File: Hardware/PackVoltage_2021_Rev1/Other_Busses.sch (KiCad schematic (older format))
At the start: 40 parts, among them Q5 Q_NMOS_DGS, Q6 Q_NMOS_DGS, Q7 Q_NMOS_DGS, Q8 Q_NMOS_DGS, U13 LT1910, U14 LT1910, U15 LT1910, U16 INA281, U17 INA281, U18 INA281, U19 LT1910, U20 INA281

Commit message: Renaming Extra Bus, Fixing Fuse Values
Renamed Extra 6 bus to Auxiliary 1 and moved it from Motor Busses to Other Busses
Changed Fuse values on Other Busses from 15 for all to 25 for Aux, Spare, and Rocket, to 10 for Vacuum, and to 20 for 12V
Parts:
- added C?: 0.1uF, symbol Device:C_Small
- added C?: 10uF, symbol Device:C_Small
- added D?: LED, symbol Device:LED
- added F?: 25, symbol Device:Fuse
- added Q?: Q_NMOS_DGS, symbol Device:Q_NMOS_DGS
- added R?: 5.1k, symbol Device:R
- added R?: 0.05, symbol Device:R
- added R?: 3300, symbol Device:R
- added U?: INA281, symbol MRDT_ICs:INA281
- added U?: LT1910, symbol MRDT_ICs:LT1910
- F5: value 15 -> 20
- F6: value 15 -> 10
- F7, F8: value 15 -> 25
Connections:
- net 5V: now also R?.2, U?.5 (V+)
- net GND: now also C?.2, C?.2, R?.2, U?.1 (GND), U?.2 (GND)
- net PV: now also F?.1
- new net: C?.1, F?.2, Q?.1 (D), U?.6 (SENSE), U?.8 (V+)
- new net: Q?.2 (G), U?.5 (GATE)
- new net: R?.1, U?.3 (FAULT)
- new net: C?.1, U?.2 (TIMER)
- new net: R?.2, U?.4 (-)
- new net: D?.1 (K), R?.1
- new net Anderson_A1: D?.2 (A), Q?.3 (S), R?.1, U?.3 (+)
- new net Current_Sensor_A1: U?.1
- new net Driver_A1: U?.4 (IN)
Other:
- note added: "Auxiliary"

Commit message: Fixed anderson connections
Mistake made when rearranging busses so they would fit on sheet fixed
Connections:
- net Anderson_A1: now also R?.2, U?.4 (-); no longer D?.2 (A), Q?.3 (S), R?.1, U?.3 (+)
- net Anderson_R1: now also R21.2, U18.4 (-); no longer D15.2 (A), Q7.3 (S), R21.1, U18.3 (+)
- net Anderson_S1: now also R26.2, U20.4 (-); no longer D16.2 (A), Q8.3 (S), R26.1, U20.3 (+)
- net Anderson_T1: now also R19.2, U16.4 (-); no longer D13.2 (A), Q5.3 (S), R19.1, U16.3 (+)
- net Anderson_V1: now also R20.2, U17.4 (-); no longer D14.2 (A), Q6.3 (S), R20.1, U17.3 (+)
- new net: D15.2 (A), Q7.3 (S), R21.1, U18.3 (+)
- new net: D14.2 (A), Q6.3 (S), R20.1, U17.3 (+)
- new net: D16.2 (A), Q8.3 (S), R26.1, U20.3 (+)
- new net: D?.2 (A), Q?.3 (S), R?.1, U?.3 (+)
- new net: D13.2 (A), Q5.3 (S), R19.1, U16.3 (+)
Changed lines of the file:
@@
 Connection ~ 3100 1850
 Wire Wire Line
-	3550 1950 3900 1950
-Wire Wire Line
-	3100 1850 3100 2100
-Wire Wire Line
-	3100 2100 3350 2100
-Connection ~ 3100 2100
-Wire Wire Line
-	3100 2100 3100 2300
+	3550 1950 3750 1950
+Wire Wire Line
+	3750 2100 4000 2100
 Text HLabel 4500 1450 1    50   Output ~ 0
 Current_Sensor_R1
@@
 Connection ~ 3050 3850
 Wire Wire Line
-	3500 3950 3850 3950
-Wire Wire Line
-	3050 3850 3050 4100
-Wire Wire Line
-	3050 4100 3300 4100
-Connection ~ 3050 4100
-Wire Wire Line
-	3050 4100 3050 4300
+	3500 3950 3700 3950
+Wire Wire Line
+	3700 4100 3950 4100
 Text HLabel 4450 3450 1    50   Output ~ 0
 Current_Sensor_T1
@@
 Connection ~ 3050 6050
 Wire Wire Line
-	3500 6150 3850 6150
-Wire Wire Line
-	3050 6050 3050 6300
-Wire Wire Line
-	3050 6300 3300 6300
-Connection ~ 3050 6300
-Wire Wire Line
-	3050 6300 3050 6500
+	3500 6150 3700 6150
+Wire Wire Line
+	3700 6300 3950 6300
 Text HLabel 4450 5650 1    50   Output ~ 0
 Current_Sensor_V1
@@
 Connection ~ 8450 1900
 Wire Wire Line
-	8900 2000 9250 2000
-Wire Wire Line
-	8450 1900 8450 2150
-Wire Wire Line
-	8450 2150 8700 2150
-Connection ~ 8450 2150
-Wire Wire Line
-	8450 2150 8450 2350
+	8900 2000 9100 2000
+Wire Wire Line
+	9100 2150 9350 2150
 Text HLabel 9850 1500 1    50   Output ~ 0
 Current_Sensor_S1
@@
 	1    0    0    -1
 $EndComp
-Text HLabel 3350 2100 2    50   Output ~ 0
+Text HLabel 4000 2100 2    50   Output ~ 0
 Anderson_R1
-Text HLabel 3300 4100 2    50   Output ~ 0
+Text HLabel 3950 4100 2    50   Output ~ 0
 Anderson_T1
-Text HLabel 3300 6300 2    50   Output ~ 0
+Text HLabel 3950 6300 2    50   Output ~ 0
 Anderson_V1
-Text HLabel 8700 2150 2    50   Output ~ 0
+Text HLabel 9350 2150 2    50   Output ~ 0
 Anderson_S1
 $Comp
@@
 Connection ~ 8450 3950
 Wire Wire Line
-	8900 4050 9250 4050
-Wire Wire Line
-	8450 3950 8450 4200
-Wire Wire Line
-	8450 4200 8700 4200
-Connection ~ 8450 4200
-Wire Wire Line
-	8450 4200 8450 4400
+	8900 4050 9100 4050
+Wire Wire Line
+	9100 4200 9350 4200
 Text HLabel 9850 3550 1    50   Output ~ 0
 Current_Sensor_A1
-Text HLabel 8700 4200 2    50   Output ~ 0
+Text HLabel 9350 4200 2    50   Output ~ 0
 Anderson_A1
+Wire Wire Line
+	3100 1850 3100 2300
+Wire Wire Line
+	3750 2100 3750 1950
+Connection ~ 3750 1950
+Wire Wire Line
+	3750 1950 3900 1950
+Wire Wire Line
+	3050 3850 3050 4300
+Wire Wire Line
+	3700 4100 3700 3950
+Connection ~ 3700 3950
+Wire Wire Line
+	3700 3950 3850 3950
+Wire Wire Line
+	3050 6050 3050 6500
+Wire Wire Line
+	3700 6300 3700 6150
+Connection ~ 3700 6150
+Wire Wire Line
+	3700 6150 3850 6150
+Wire Wire Line
+	8450 3950 8450 4400
+Wire Wire Line
+	9100 4200 9100 4050
+Connection ~ 9100 4050
+Wire Wire Line
+	9100 4050 9250 4050
+Wire Wire Line
+	8450 1900 8450 2350
+Wire Wire Line
+	9100 2150 9100 2000
+Connection ~ 9100 2000
+Wire Wire Line
+	9100 2000 9250 2000
 $EndSCHEMATC

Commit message: updated busses, fuses, and some names
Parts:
- F7: value 25 -> 15
- F8: value 25 -> 20
- F9: renamed from F?; value 25 -> 20
- gave numbers to parts that had none: 8
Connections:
- net Anderson_S1 renamed Anderson_D1
- net Current_Sensor_S1 renamed Current_Sensor_D1
- net Driver_E1 renamed Driver_V1
- net Driver_S1 renamed Driver_D1
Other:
- note added: "Driveboard"
- note removed: "Spare"
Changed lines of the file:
@@
 $Descr A4 11693 8268
 encoding utf-8
-Sheet 5 5
+Sheet 4 5
 Title ""
 Date ""
@@
 	4450 5750 4450 5650
 Text HLabel 1050 5850 0    50   Input ~ 0
-Driver_E1
+Driver_V1
 Wire Wire Line
 	3050 6050 3300 6050
@@
 AR Path="/5F8EFCC9/5F8B2B23" Ref="F8"  Part="1"
 F 0 "F8" V 7750 1250 50  0000 L CNN
-F 1 "25" V 7850 1250 50  0000 L CNN
+F 1 "20" V 7850 1250 50  0000 L CNN
 F 2 "" V 7780 1300 50  0001 C CNN
 F 3 "~" H 7850 1300 50  0001 C CNN
@@
 Connection ~ 7950 1550
 Text Notes 7500 900  0    157  ~ 0
-Spare
+Driveboard
 Wire Wire Line
 	8700 1900 8700 1500
@@
 	9850 1600 9850 1500
 Text HLabel 6450 1700 0    50   Input ~ 0
-Driver_S1
+Driver_D1
 Wire Wire Line
 	8450 1900 8700 1900
@@
 	9100 2150 9350 2150
 Text HLabel 9850 1500 1    50   Output ~ 0
-Current_Sensor_S1
+Current_Sensor_D1
 $Comp
 L Device:Fuse F?
@@
 AR Path="/5F8EFCC9/5F78099C" Ref="F7"  Part="1"
 F 0 "F7" V 2400 1200 50  0000 L CNN
-F 1 "25" V 2500 1200 50  0000 L CNN
+F 1 "15" V 2500 1200 50  0000 L CNN
 F 2 "" V 2430 1250 50  0001 C CNN
 F 3 "~" H 2500 1250 50  0001 C CNN
@@
 Anderson_V1
 Text HLabel 9350 2150 2    50   Output ~ 0
-Anderson_S1
+Anderson_D1
 $Comp
 L Device:Q_NMOS_DGS Q?
@@
 P 7850 3350
 AR Path="/5F7A6A8B/5F8E41F3" Ref="F?"  Part="1"
-AR Path="/5F8EFCC9/5F8E41F3" Ref="F?"  Part="1"
-F 0 "F?" V 7750 3300 50  0000 L CNN
-F 1 "25" V 7850 3300 50  0000 L CNN
+AR Path="/5F8EFCC9/5F8E41F3" Ref="F9"  Part="1"
+F 0 "F9" V 7750 3300 50  0000 L CNN
+F 1 "20" V 7850 3300 50  0000 L CNN
 F 2 "" V 7780 3350 50  0001 C CNN
 F 3 "~" H 7850 3350 50  0001 C CNN
@@
 P 6300 3600
 AR Path="/5F7A6A8B/5F8E41F9" Ref="R?"  Part="1"
-AR Path="/5F8EFCC9/5F8E41F9" Ref="R?"  Part="1"
-F 0 "R?" V 6200 3600 50  0000 C CNN
+AR Path="/5F8EFCC9/5F8E41F9" Ref="R28"  Part="1"
+F 0 "R28" V 6200 3600 50  0000 C CNN
 F 1 "5.1k" V 6300 3600 50  0000 C CNN
 F 2 "" V 6230 3600 50  0001 C CNN
@@
 P 6600 4100
 AR Path="/5F7A6A8B/5F8E4206" Ref="C?"  Part="1"
-AR Path="/5F8EFCC9/5F8E4206" Ref="C?"  Part="1"
-F 0 "C?" H 6692 4146 50  0000 L CNN
+AR Path="/5F8EFCC9/5F8E4206" Ref="C27"  Part="1"
+F 0 "C27" H 6692 4146 50  0000 L CNN
 F 1 "0.1uF" H 6692 4055 50  0000 L CNN
 F 2 "" H 6600 4100 50  0001 C CNN
@@
 P 7950 4100
 AR Path="/5F7A6A8B/5F8E420E" Ref="C?"  Part="1"
-AR Path="/5F8EFCC9/5F8E420E" Ref="C?"  Part="1"
-F 0 "C?" H 8042 4146 50  0000 L CNN
+AR Path="/5F8EFCC9/5F8E420E" Ref="C28"  Part="1"
+F 0 "C28" H 8042 4146 50  0000 L CNN
 F 1 "10uF" H 8042 4055 50  0000 L CNN
 F 2 "" H 7950 4100 50  0001 C CNN
@@
 P 8900 3800
 AR Path="/5F7A6A8B/5F8E4229" Ref="R?"  Part="1"
-AR Path="/5F8EFCC9/5F8E4229" Ref="R?"  Part="1"
-F 0 "R?" V 8800 3750 50  0000 L CNN
+AR Path="/5F8EFCC9/5F8E4229" Ref="R29"  Part="1"
+F 0 "R29" V 8800 3750 50  0000 L CNN
 F 1 "0.05" V 8900 3700 50  0000 L CNN
 F 2 "" V 8830 3800 50  0001 C CNN
@@
 P 8850 4400
 AR Path="/5F7A6A8B/5F8E4236" Ref="D?"  Part="1"
-AR Path="/5F8EFCC9/5F8E4236" Ref="D?"  Part="1"
-F 0 "D?" H 8850 4500 50  0000 C CNN
+AR Path="/5F8EFCC9/5F8E4236" Ref="D17"  Part="1"
+F 0 "D17" H 8850 4500 50  0000 C CNN
 F 1 "LED" H 8850 4600 50  0000 C CNN
 F 2 "" H 8850 4400 50  0001 C CNN
@@
 P 9300 4400
 AR Path="/5F7A6A8B/5F8E423D" Ref="R?"  Part="1"
-AR Path="/5F8EFCC9/5F8E423D" Ref="R?"  Part="1"
-F 0 "R?" V 9200 4350 50  0000 L CNN
+AR Path="/5F8EFCC9/5F8E423D" Ref="R30"  Part="1"
+F 0 "R30" V 9200 4350 50  0000 L CNN
 F 1 "3300" V 9300 4300 50  0000 L CNN
 F 2 "" V 9230 4400 50  0001 C CNN
@@
 P 9450 3650
 AR Path="/5F7A6A8B/5F8E4246" Ref="U?"  Part="1"
-AR Path="/5F8EFCC9/5F8E4246" Ref="U?"  Part="1"
-F 0 "U?" H 9550 3950 50  0000 L CNN
+AR Path="/5F8EFCC9/5F8E4246" Ref="U22"  Part="1"
+F 0 "U22" H 9550 3950 50  0000 L CNN
 F 1 "INA281" H 9500 3850 50  0000 L CNN
 F 2 "" H 9700 3850 50  0001 C CNN
@@
 P 6800 4000
 AR Path="/5F7A6A8B/5F8E424C" Ref="U?"  Part="1"
-AR Path="/5F8EFCC9/5F8E424C" Ref="U?"  Part="1"
-F 0 "U?" H 7175 4687 60  0000 C CNN
+AR Path="/5F8EFCC9/5F8E424C" Ref="U21"  Part="1"
+F 0 "U21" H 7175 4687 60  0000 C CNN
 F 1 "LT1910" H 7175 4581 60  0000 C CNN
 F 2 "" H 6800 4000 60  0001 C CNN

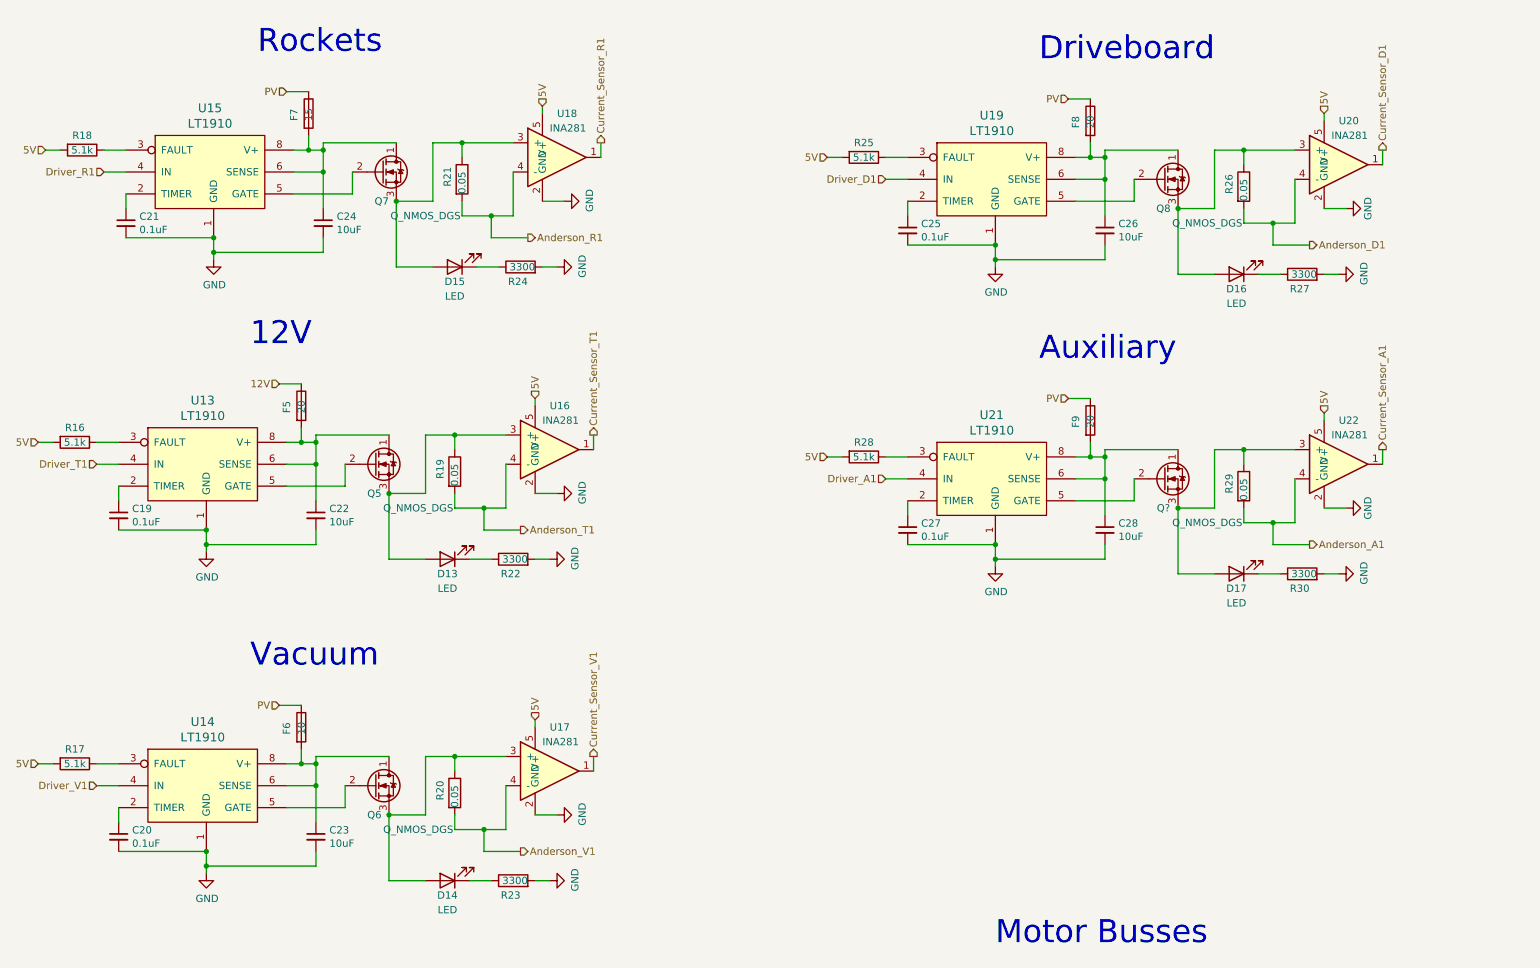
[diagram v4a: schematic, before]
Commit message: corrected orientation of ground symbols, renamed buck converters, still need to update tiva with extra 12V pin
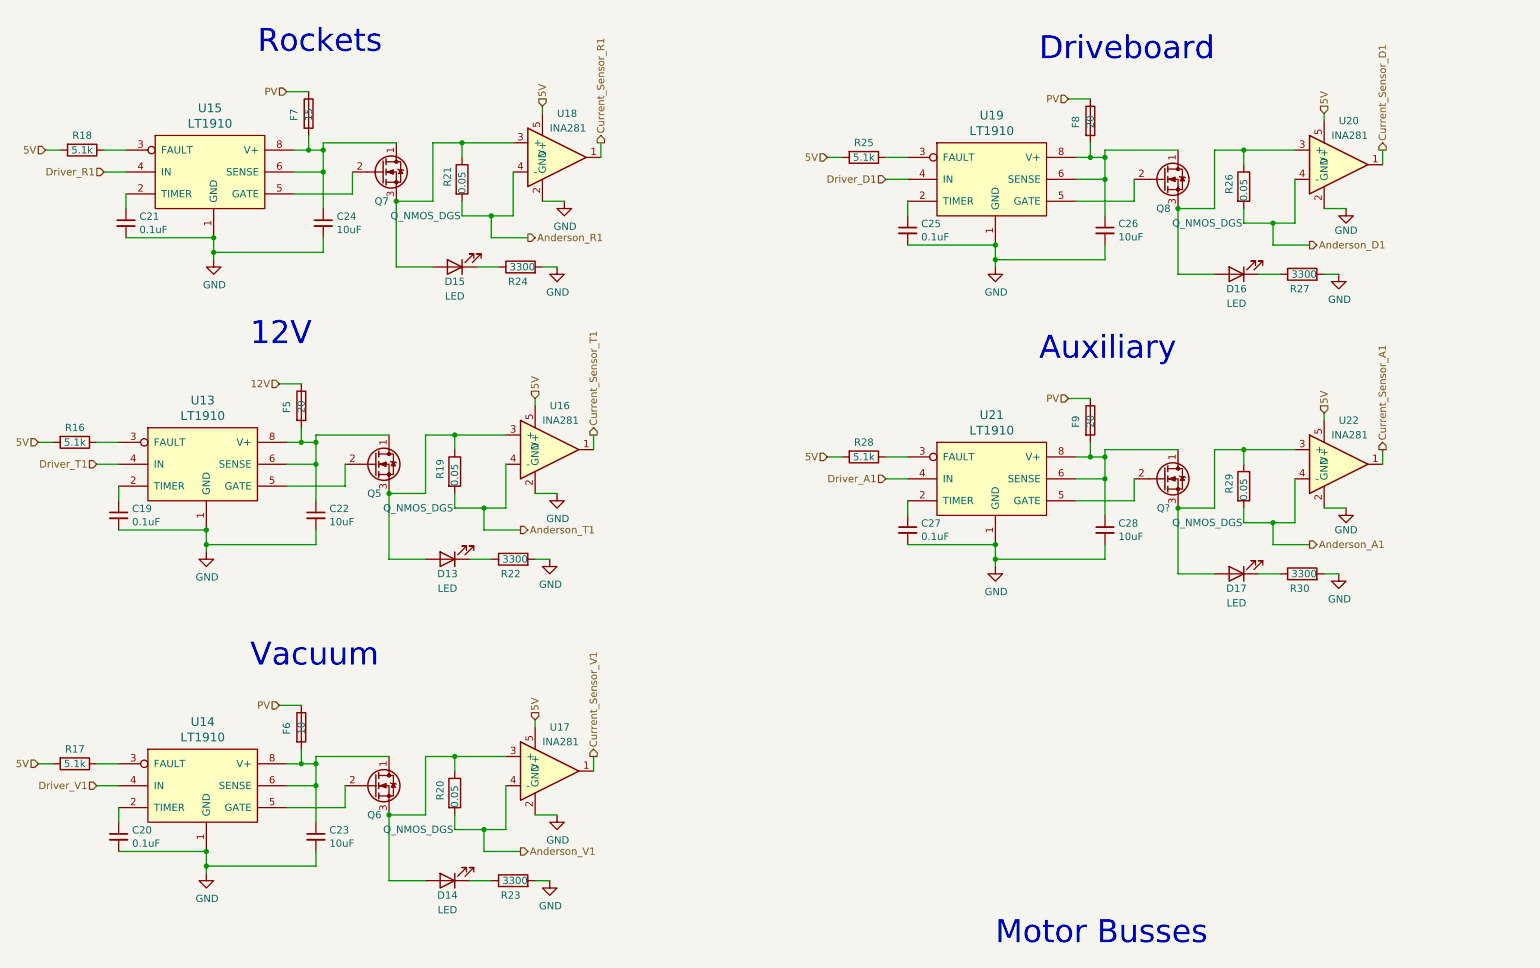
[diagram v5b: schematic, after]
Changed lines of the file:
@@
 F 3 "" H 4250 1850 50  0001 C CNN
 	1    4250 1850
-	0    -1   -1   0
+	1    0    0    -1
 $EndComp
 $Comp
@@
 F 3 "" H 4200 2300 50  0001 C CNN
 	1    4200 2300
-	0    -1   -1   0
+	1    0    0    -1
 $EndComp
 Connection ~ 3100 1850
@@
 F 3 "" H 4200 3850 50  0001 C CNN
 	1    4200 3850
-	0    -1   -1   0
+	1    0    0    -1
 $EndComp
 $Comp
@@
 F 3 "" H 4150 4300 50  0001 C CNN
 	1    4150 4300
-	0    -1   -1   0
+	1    0    0    -1
 $EndComp
 Connection ~ 3050 3850
@@
 F 3 "" H 4200 6050 50  0001 C CNN
 	1    4200 6050
-	0    -1   -1   0
+	1    0    0    -1
 $EndComp
 $Comp
@@
 F 3 "" H 4150 6500 50  0001 C CNN
 	1    4150 6500
-	0    -1   -1   0
+	1    0    0    -1
 $EndComp
 Connection ~ 3050 6050
@@
 F 3 "" H 9600 1900 50  0001 C CNN
 	1    9600 1900
-	0    -1   -1   0
+	1    0    0    -1
 $EndComp
 $Comp
@@
 F 3 "" H 9550 2350 50  0001 C CNN
 	1    9550 2350
-	0    -1   -1   0
+	1    0    0    -1
 $EndComp
 Connection ~ 8450 1900
@@
 F 3 "" H 9600 3950 50  0001 C CNN
 	1    9600 3950
-	0    -1   -1   0
+	1    0    0    -1
 $EndComp
 $Comp
@@
 F 3 "" H 9550 4400 50  0001 C CNN
 	1    9550 4400
-	0    -1   -1   0
+	1    0    0    -1
 $EndComp
 Connection ~ 8450 3950

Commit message: Updated molex connector (Still need tiva pin)
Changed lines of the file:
@@
 Wire Wire Line
 	3350 1850 3350 1450
-Wire Wire Line
-	3550 1450 3900 1450
 Connection ~ 3550 1450
 Wire Wire Line
@@
 	1    0    0    -1
 $EndComp
-Wire Wire Line
-	4100 1850 4250 1850
 $Comp
 L power:GND #PWR?
@@
 Wire Wire Line
 	4100 2300 4200 2300
-Text HLabel 2350 1100 0    50   Input ~ 0
+Text HLabel 2350 1100 1    50   Input ~ 0
 PV
-$Comp
-L MRDT_ICs:INA281 U?
-U 1 1 5F9AF7BB
-P 4100 1550
-AR Path="/5F7A6A8B/5F9AF7BB" Ref="U?"  Part="1"
-AR Path="/5F8EFCC9/5F9AF7BB" Ref="U18"  Part="1"
-F 0 "U18" H 4200 1850 50  0000 L CNN
-F 1 "INA281" H 4150 1750 50  0000 L CNN
-F 2 "" H 4350 1750 50  0001 C CNN
-F 3 "" H 4350 1750 50  0001 C CNN
-	1    4100 1550
-	1    0    0    -1
-$EndComp
 $Comp
 L MRDT_ICs:LT1910 U?
@@
 Text HLabel 4100 1200 1    50   Input ~ 0
 5V
-Text HLabel 700  1500 0    50   Input ~ 0
-5V
 Wire Wire Line
 	700  1500 800  1500
 Wire Wire Line
 	4100 1200 4100 1250
-Wire Wire Line
-	4500 1550 4500 1450
 Text HLabel 1100 1650 0    50   Input ~ 0
 Driver_R1
@@
 Wire Wire Line
 	3750 2100 4000 2100
-Text HLabel 4500 1450 1    50   Output ~ 0
-Current_Sensor_R1
 $Comp
 L Device:Q_NMOS_DGS Q?
@@
 Wire Wire Line
 	4050 4300 4150 4300
-Text HLabel 2300 3100 0    50   Input ~ 0
+Text HLabel 2300 3100 1    50   Input ~ 0
 12V
 $Comp
@@
 Text HLabel 4050 3200 1    50   Input ~ 0
 5V
-Text HLabel 650  3500 0    50   Input ~ 0
-5V
 Wire Wire Line
 	650  3500 750  3500
 Wire Wire Line
 	4050 3200 4050 3250
-Wire Wire Line
-	4450 3550 4450 3450
 Text HLabel 1050 3650 0    50   Input ~ 0
 Driver_T1
@@
 Wire Wire Line
 	3700 4100 3950 4100
-Text HLabel 4450 3450 1    50   Output ~ 0
+Text HLabel 4550 3550 2    50   Output ~ 0
 Current_Sensor_T1
 $Comp
@@
 Wire Wire Line
 	4050 6500 4150 6500
-Text HLabel 2300 5300 0    50   Input ~ 0
+Text HLabel 2300 5300 1    50   Input ~ 0
 PV
 $Comp
@@
 Text HLabel 4050 5400 1    50   Input ~ 0
 5V
-Text HLabel 650  5700 0    50   Input ~ 0
-5V
 Wire Wire Line
 	650  5700 750  5700
 Wire Wire Line
 	4050 5400 4050 5450
-Wire Wire Line
-	4450 5750 4450 5650
 Text HLabel 1050 5850 0    50   Input ~ 0
 Driver_V1
@@
 Wire Wire Line
 	3700 6300 3950 6300
-Text HLabel 4450 5650 1    50   Output ~ 0
+Text HLabel 4550 5750 2    50   Output ~ 0
 Current_Sensor_V1
 $Comp
@@
 Wire Wire Line
 	9450 2350 9550 2350
-Text HLabel 7700 1150 0    50   Input ~ 0
+Text HLabel 7700 1150 1    50   Input ~ 0
 PV
 $Comp
@@
 Text HLabel 9450 1250 1    50   Input ~ 0
 5V
-Text HLabel 6050 1550 0    50   Input ~ 0
-5V
 Wire Wire Line
 	6050 1550 6150 1550
 Wire Wire Line
 	9450 1250 9450 1300
-Wire Wire Line
-	9850 1600 9850 1500
 Text HLabel 6450 1700 0    50   Input ~ 0
 Driver_D1
@@
 Wire Wire Line
 	9100 2150 9350 2150
-Text HLabel 9850 1500 1    50   Output ~ 0
+Text HLabel 9950 1600 2    50   Output ~ 0
 Current_Sensor_D1
 $Comp
@@
 Wire Wire Line
 	9450 4400 9550 4400
-Text HLabel 7700 3200 0    50   Input ~ 0
+Text HLabel 7700 3200 1    50   Input ~ 0
 PV
 $Comp
@@
 Text HLabel 9450 3300 1    50   Input ~ 0
 5V
-Text HLabel 6050 3600 0    50   Input ~ 0
-5V
 Wire Wire Line
 	6050 3600 6150 3600
 Wire Wire Line
 	9450 3300 9450 3350
-Wire Wire Line
-	9850 3650 9850 3550
 Text HLabel 6450 3750 0    50   Input ~ 0
 Driver_A1
@@
 Wire Wire Line
 	9100 4200 9350 4200
-Text HLabel 9850 3550 1    50   Output ~ 0
+Text HLabel 9950 3650 2    50   Output ~ 0
 Current_Sensor_A1
 Text HLabel 9350 4200 2    50   Output ~ 0
@@
 Wire Wire Line
 	9100 2000 9250 2000
+Text HLabel 700  1150 1    50   Input ~ 0
+5V
+Wire Wire Line
+	700  1150 700  1500
+Text HLabel 650  3150 1    50   Input ~ 0
+5V
+Wire Wire Line
+	650  3150 650  3500
+Text HLabel 650  5350 1    50   Input ~ 0
+5V
+Wire Wire Line
+	650  5350 650  5700
+Text HLabel 6050 3250 1    50   Input ~ 0
+5V
+Wire Wire Line
+	6050 3250 6050 3600
+Text HLabel 6050 1200 1    50   Input ~ 0
+5V
+Wire Wire Line
+	6050 1200 6050 1550
+Wire Wire Line
+	4100 1850 4250 1850
+Text HLabel 4600 1550 2    50   Output ~ 0
+Current_Sensor_R1
+Wire Wire Line
+	3550 1450 3900 1450
+$Comp
+L MRDT_ICs:INA281 U?
+U 1 1 5F9AF7BB
+P 4100 1550
+AR Path="/5F7A6A8B/5F9AF7BB" Ref="U?"  Part="1"
+AR Path="/5F8EFCC9/5F9AF7BB" Ref="U18"  Part="1"
+F 0 "U18" H 4200 1850 50  0000 L CNN
+F 1 "INA281" H 4150 1750 50  0000 L CNN
+F 2 "" H 4350 1750 50  0001 C CNN
+F 3 "" H 4350 1750 50  0001 C CNN
+	1    4100 1550
+	1    0    0    -1
+$EndComp
+Wire Wire Line
+	4500 1550 4600 1550
+Wire Wire Line
+	9950 1600 9850 1600
+Wire Wire Line
+	9850 3650 9950 3650
+Wire Wire Line
+	4450 5750 4550 5750
+Wire Wire Line
+	4450 3550 4550 3550
 $EndSCHEMATC

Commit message: Rearranged Bucks and Fixed 12V Bus LED Resistor
Moved 5v bus to the middle and 3.3V bus to the bottom to make things more clear.
12 bus had 3300 ohm resistor when it should have 1200 ohm b/c it only has 12 V going into it
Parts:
- R22: value 3300 -> 1200
